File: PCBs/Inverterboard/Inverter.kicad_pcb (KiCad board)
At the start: 2 copper layers, 66 x 71.8 mm, 54 parts, among them IC1 L6494LDTR, J1 Conn_02x02_Odd_Even, U1 IPT015N10N5ATMA1, U2 IPT015N10N5ATMA1, U3 IPT015N10N5ATMA1, U4 IPT015N10N5ATMA1

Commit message: change in gate resistor
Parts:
- moved R9 1.39 mm to (91.2, 116.7), turned to 180 degrees
- moved R8 1.37 mm to (102.6, 116.7), turned to 180 degrees
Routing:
- net Net-(R4-Pad1): track 40.9 -> 34.8 mm

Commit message: Made final Gerber files for all boards.
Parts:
- U** (x9): footprint KiCad:7466203R -> ElectricGoKart:7466203R
- U1, U2, U3, U4: value IPT015N10N5ATMA1 -> PG-HSOF-8-1_INF
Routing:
- net GND: track 41.6 -> 0.00 mm
- net PHASE: track 22.7 -> 6.85 mm
- net +BATT: track 1.50 -> 0.00 mm
- net Net-(R4-Pad1): track 34.8 -> 34.0 mm
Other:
- board text added: "Inverter Board Spring 2021 Group 1 University of Southern Denmark"

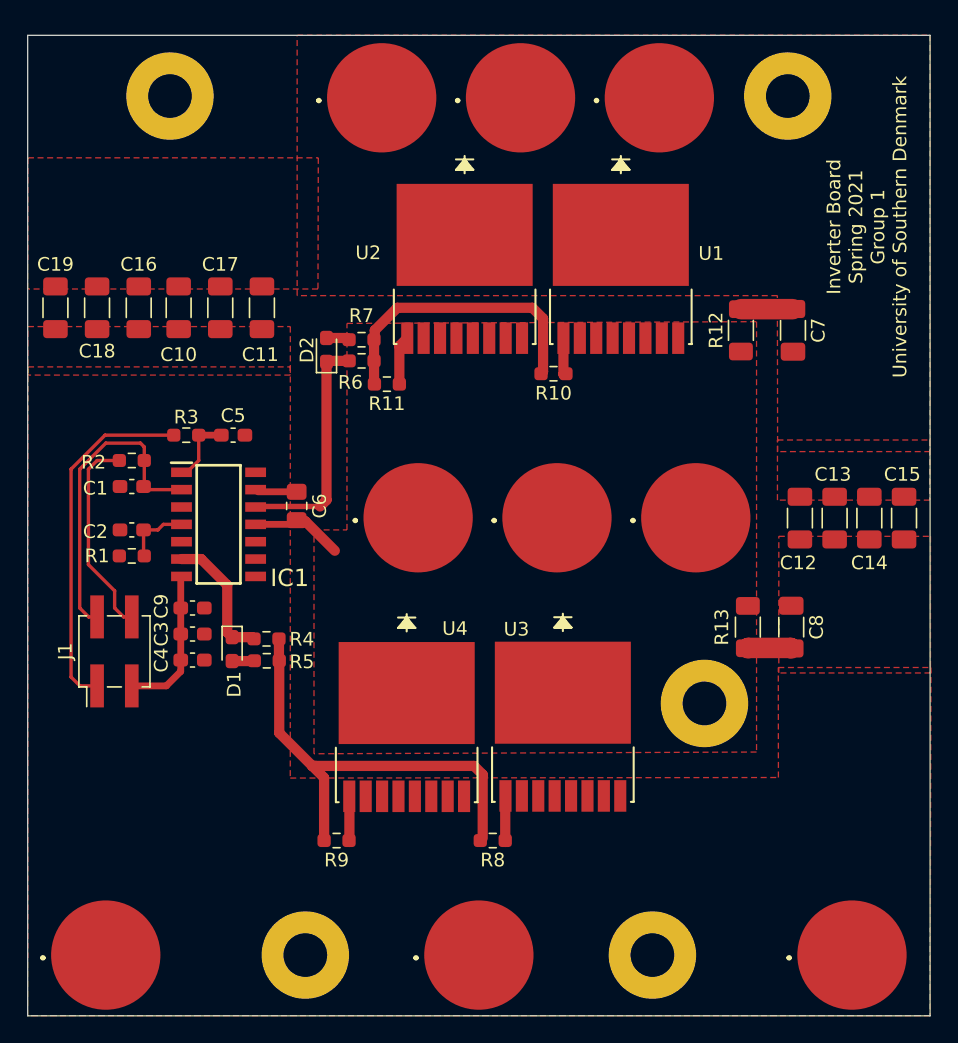
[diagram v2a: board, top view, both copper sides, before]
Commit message: Changed Inverter holes so they're good for aluminium. New Gerbers.
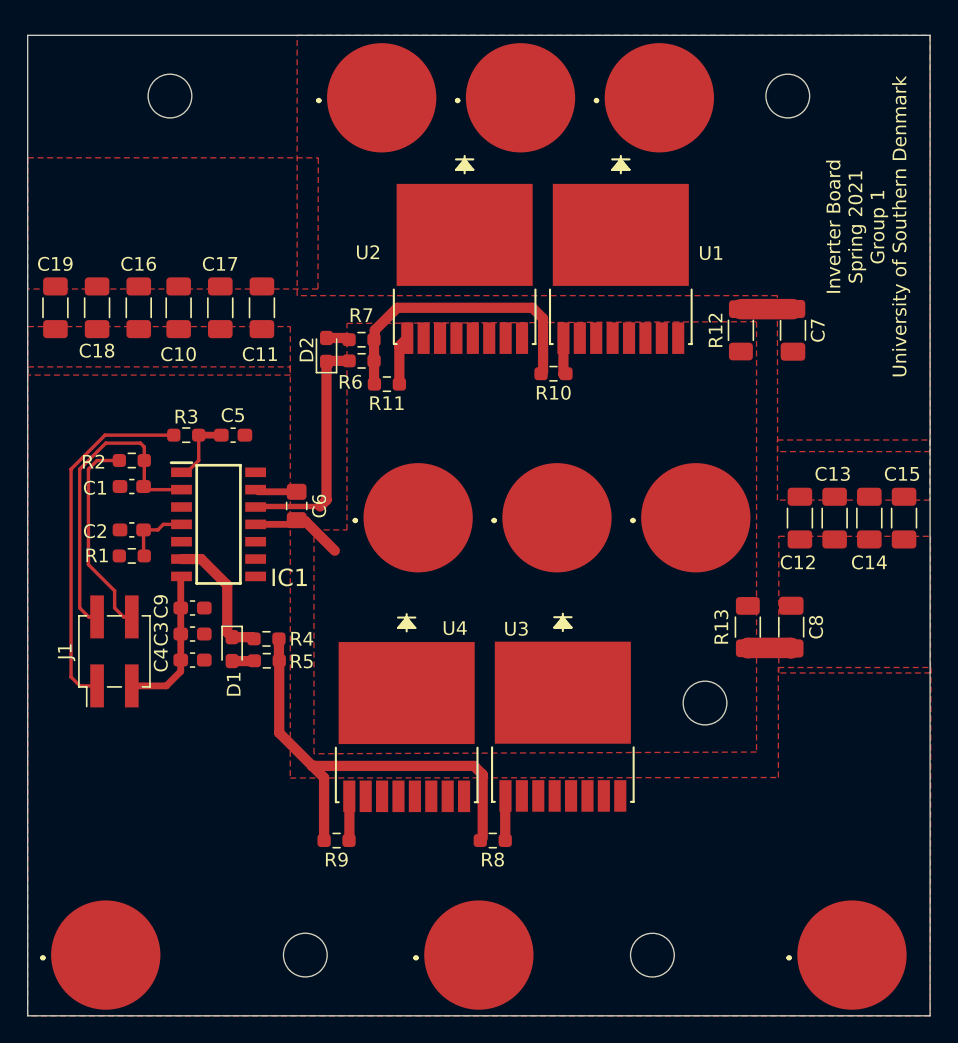
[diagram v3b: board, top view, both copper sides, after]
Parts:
- removed the REF** at (118.1, 106.7)
- removed the REF** at (79.0, 62.2)
- removed the REF** at (124.2, 62.2)
- removed the REF** at (114.3, 125.1)
- removed the REF** at (88.9, 125.1)
- added REF**: MountingHole_3.2mm_M3, MountingHole:MountingHole_3.2mm_M3, F.Cu at (88.9, 125.1)
- added REF**: MountingHole_3.2mm_M3, MountingHole:MountingHole_3.2mm_M3, F.Cu at (114.3, 125.1)
- added REF**: MountingHole_3.2mm_M3, MountingHole:MountingHole_3.2mm_M3, F.Cu at (118.2, 106.7)
- added REF**: MountingHole_3.2mm_M3, MountingHole:MountingHole_3.2mm_M3, F.Cu at (79.0, 62.2)
- added REF**: MountingHole_3.2mm_M3, MountingHole:MountingHole_3.2mm_M3, F.Cu at (124.2, 62.2)
